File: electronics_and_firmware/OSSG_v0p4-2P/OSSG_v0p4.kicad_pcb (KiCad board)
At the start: 4 copper layers, 85 x 9 mm, 72 parts, among them J1 Conn_01x05_Male, J2 Ext RGB, J3 USB_B_Micro, J4 Touch, Q1 2SC4617R BR, Q2 2SC4617R BR, Q3 PMZ290UNE2YL, Q4 YJQD30P02A, SW1 SW_SPST, SW2 Power, U1 MP23DB01HPTR, U2 ESP32-PICO-D4, U3 CH9102F, U4 XC61CC3002MR, U5 AP5054HTC, U6 MAX17048, U7 NCP167BMX330TBG, U8 SY7088

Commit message: small changes to tracks
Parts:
- moved C17 8.55 mm to (138.9, 76.4)
- moved C1 0.30 mm to (95.8, 80.3)
- moved R1 0.30 mm to (95.8, 81.3)
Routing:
- net BATT1-: track 77.6 -> 85.6 mm, vias 107 -> 123
- net Net-(Q3-Pad3): track 10.8 -> 14.1 mm
- net Net-(C15-Pad1): track 23.8 -> 20.6 mm
- net SCL: track 62.5 -> 60.9 mm
- net BATT+: track 78.4 -> 79.8 mm
- net +5V: track 79.1 -> 80.2 mm

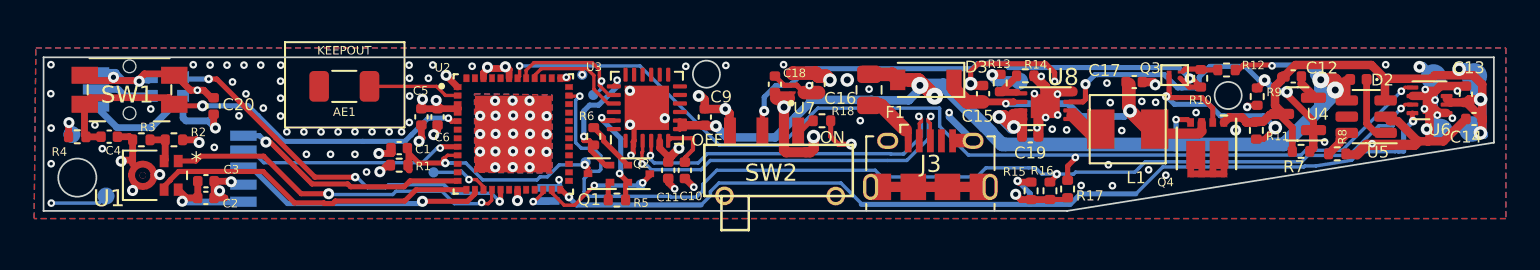
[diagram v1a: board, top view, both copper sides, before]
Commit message: ESP32 footprint edited, HUD connection, USB connector moved
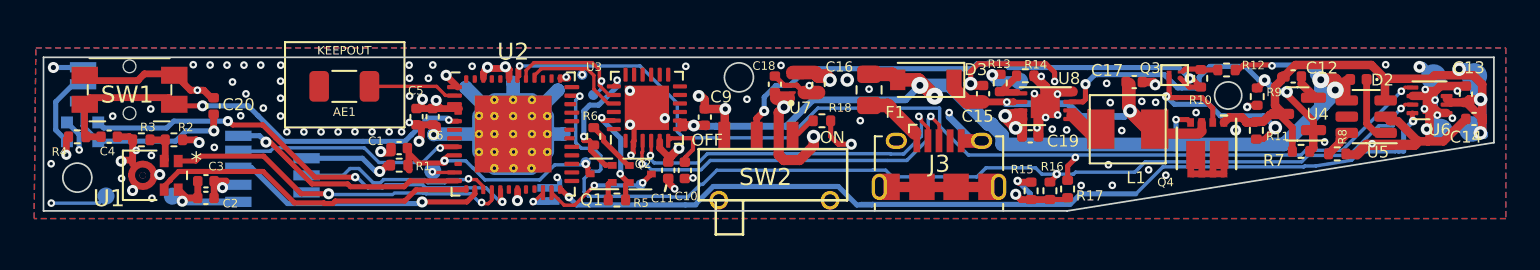
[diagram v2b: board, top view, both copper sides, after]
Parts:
- added J5: Ext. HUD (experimental), OSSG_footprints:Solder-3P-Connector, B.Cu at (90.4, 81.4)
- TP1: value IO26 -> IO35; footprint OSSG_footprints:Breakout_pads_very_small -> OSSG_footprints:Breakout_pads_small
- U2: footprint OSSG_footprints:ESP32_PICO_D4 -> OSSG_footprints:OSSG_ESP32-Pico_D4
- moved TP8 6.91 mm to (82.6, 83.1)
- moved D1 5.64 mm to (77.3, 79.4)
- moved J2 0.82 mm to (77.3, 77.1)
- moved J3 0.51 mm to (127.5, 81.3)
- moved SW2 0.42 mm to (113.4, 80.4)
- moved J1 0.30 mm to (86.4, 82.0)
- moved C5 0.29 mm to (96.9, 78.5)
- moved C6 0.29 mm to (97.8, 78.5)
- moved Q1 0.14 mm to (107.7, 81.8)
- moved TP1 0.10 mm to (97.8, 81.7)
- moved Q2 0.10 mm to (110.0, 81.8)
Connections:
- TP1 pad 1: DAC -> IO35
- U2 pad 11: SPARE -> IO35
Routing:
- net BATT1-: track 85.6 -> 151.4 mm, vias 123 -> 97
- net DAC: track 3.53 -> 11.5 mm
- net +3V3: track 32.4 -> 37.2 mm
- net RGB: track 22.4 -> 26.7 mm
- net IO35: track 0.00 -> 1.31 mm, vias 0 -> 1
- net Net-(D1-Pad1): track 3.43 -> 4.61 mm
- net EN: track 15.1 -> 14.2 mm
- net ALRT: track 60.9 -> 61.5 mm
- net Net-(Q3-Pad1): track 35.7 -> 36.3 mm
- removed copper zone on B.Cu, net +5V
- removed copper zone on F.Cu, net +5V
- removed copper zone on In1.Cu, net +5V
- removed copper zone on In2.Cu, net +5V
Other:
- outline, holes or cut-outs redrawn
- board text added: "DAC"
- board text added: "Ext. LED"
- board text added: "HUD"
- board text added: "M1.6"
- board text removed: "LED"
- board text removed: "M2.25"
